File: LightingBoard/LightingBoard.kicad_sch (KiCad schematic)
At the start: 58 parts, among them J1 Barrel_Jack_Switch, J2 LED Out, J3 LED Out, J4 Programming, J5 UART, U1 AP7384-50SA, U2 NCV833, U3 INA180A2, U4 LMR33630ADDA, U5 MCP4725xxx-xCH, U6 INA180A2, U7 LMR33630ADDA, U8 MCP4725xxx-xCH, U9 ATtiny2313A-S

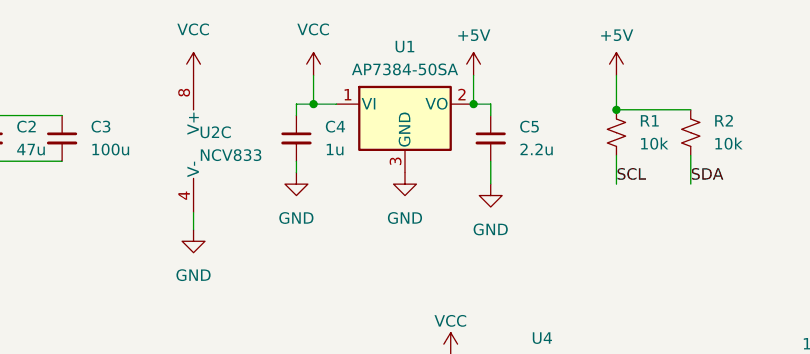
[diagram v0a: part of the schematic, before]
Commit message: add cost estimates
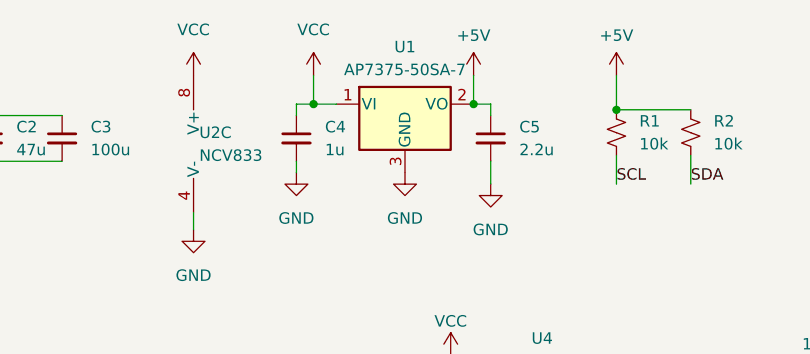
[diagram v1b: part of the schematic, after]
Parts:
- C1, C11, C12, C13, C14, C15, C17, C18, C4, C5, C6, C7, C8, C9, D1: Cost (none) -> .01
- C10, C16, C3: Cost (none) -> .183
- C2: Cost (none) -> 0
- L2, L4: Cost (none) -> .364
- R1, R10, R11, R13, R14, R15, R16, R17, R18, R19, R2, R20, R21, R4, R5, R6, R7, R8, R9: Cost (none) -> .005
- R12, R3: Cost (none) -> .052
- U1: value AP7384-50SA -> AP7375-50SA-7; Cost (none) -> .10
- U2: Cost (none) -> .225
- U3, U6: Cost (none) -> .131
- U4, U7: Cost (none) -> .927
- U5, U8: Cost (none) -> .949
- U9: Cost (none) -> 1.27

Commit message: NO MORR DINOSAURR
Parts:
- removed U1: AP7375-50SA-7, Package_TO_SOT_SMD:SOT-23, symbol Regulator_Linear:AP7384-50SA
- removed U9: ATtiny2313A-S, Package_SO:SOIC-20W_7.5x12.8mm_P1.27mm, symbol MCU_Microchip_ATtiny:ATtiny2313A-S
- added U10: AP2120N-5.0TRG1, Package_TO_SOT_SMD:SOT-23, symbol Regulator_Linear:MCP1700x-500xxTT
- added U9: ATtiny841-SS, Package_SO:SOIC-14_3.9x8.7mm_P1.27mm, symbol MCU_Microchip_ATtiny:ATtiny841-SS
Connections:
- net +5V: now also R11.2, U10.2 (VO), U9.1 (VCC); no longer R11.1
- net Enable1: now also U9.10 (PA3)
- net Enable2: now also U9.3 (XTAL2/PB1)
- net GND: now also C18.1, U10.1 (GND), U9.14 (GND); no longer C18.2
- net PG1: now also U9.13 (AREF/PA0)
- net PG2: now also U9.2 (XTAL1/PB0)
- net Reset: now also C18.2, R11.1, R20.2, U9.4 (~{RESET}/PB3); no longer C18.1, R11.2, R20.1
- net SCL: now also J4.2 (Pin_2), U9.9 (PA4); no longer J4.5 (Pin_5)
- net SDA: now also J4.4 (Pin_4), U9.7 (PA6); no longer J4.3 (Pin_3)
- net Status: now also U9.5 (PB2)
- net UART_RX: now also U9.11 (PA2)
- net UART_TX: now also U9.12 (PA1)
- net VCC: now also U10.3 (VI)
- new net CS(10): J4.5 (Pin_5), R20.1
- new net MISO(12): J4.3 (Pin_3), U9.8 (PA5)
- no-connect marks 6 -> 2
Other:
- moved on the sheet: C18, J4, J5, R11, R20

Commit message: fix some issues
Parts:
- C12, C6: value .1u -> 100nF
- R14, R5: value 4k -> 30k
- R18, R9: value 1k -> 10k
- U2: value NCV833 -> TL5580IDR
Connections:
- net +5V: now also C12.1, C6.1, U3.5 (V+), U6.5 (V+)
- net VCC: no longer C12.1, C6.1, U3.5 (V+), U6.5 (V+)
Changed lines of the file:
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@@
       (effects (font (size 1.27 1.27)) (justify left))
     )
-    (property "Value" ".1u" (at 205.74 113.6713 0)
+    (property "Value" "100nF" (at 205.74 113.6713 0)
       (effects (font (size 1.27 1.27)) (justify left))
     )
@@
       (effects (font (size 1.27 1.27)) (justify right))
     )
-    (property "Value" "4k" (at 276.225 133.985 0)
+    (property "Value" "30k" (at 276.225 133.985 0)
       (effects (font (size 1.27 1.27)) (justify right))
     )
@@
       (effects (font (size 1.27 1.27)) hide)
     )
-    (property "Datasheet" "~" (at 274.32 132.715 0)
+    (property "Datasheet" "RT0603FRE0730KL " (at 274.32 132.715 0)
       (effects (font (size 1.27 1.27)) hide)
     )
@@
         (path "/3512c088-bc62-4a72-803d-5db96724f2eb"
           (reference "#PWR025") (unit 1)
-        )
-      )
-    )
-  )
-  (symbol (lib_id "power:VCC") (at 195.58 49.53 0) (unit 1)
-    (in_bom yes) (on_board yes) (dnp no)
-    (property "Reference" "#PWR014" (at 195.58 53.34 0)
-      (effects (font (size 1.27 1.27)) hide)
-    )
-    (property "Value" "VCC" (at 195.58 45.72 0)
-      (effects (font (size 1.27 1.27)))
-    )
-    (property "Footprint" "" (at 195.58 49.53 0)
-      (effects (font (size 1.27 1.27)) hide)
-    )
-    (property "Datasheet" "" (at 195.58 49.53 0)
-      (effects (font (size 1.27 1.27)) hide)
-    )
-    (pin "1")
-    (instances
-      (project "LightingBoard"
-        (path "/3512c088-bc62-4a72-803d-5db96724f2eb"
-          (reference "#PWR014") (unit 1)
         )
       )
@@
       (effects (font (size 1.27 1.27)) (justify right))
     )
-    (property "Value" "1k" (at 274.955 74.295 0)
+    (property "Value" "10k" (at 274.955 74.295 0)
       (effects (font (size 1.27 1.27)) (justify right))
     )
@@
     )
   )
-  (symbol (lib_id "power:VCC") (at 201.295 41.275 0) (unit 1)
-    (in_bom yes) (on_board yes) (dnp no)
-    (property "Reference" "#PWR011" (at 201.295 45.085 0)
-      (effects (font (size 1.27 1.27)) hide)
-    )
-    (property "Value" "VCC" (at 201.295 37.465 0)
-      (effects (font (size 1.27 1.27)))
-    )
-    (property "Footprint" "" (at 201.295 41.275 0)
-      (effects (font (size 1.27 1.27)) hide)
-    )
-    (property "Datasheet" "" (at 201.295 41.275 0)
-      (effects (font (size 1.27 1.27)) hide)
-    )
-    (pin "1")
-    (instances
-      (project "LightingBoard"
-        (path "/3512c088-bc62-4a72-803d-5db96724f2eb"
-          (reference "#PWR011") (unit 1)
-        )
-      )
-    )
-  )
   (symbol (lib_id "Device:C_Small") (at 162.56 130.81 0) (unit 1)
     (in_bom yes) (on_board yes) (dnp no) (fields_autoplaced)
@@
     )
   )
+  (symbol (lib_id "power:+5V") (at 196.85 118.11 0) (unit 1)
+    (in_bom yes) (on_board yes) (dnp no) (fields_autoplaced)
+    (property "Reference" "#PWR011" (at 196.85 121.92 0)
+      (effects (font (size 1.27 1.27)) hide)
+    )
+    (property "Value" "+5V" (at 196.85 113.665 0)
+      (effects (font (size 1.27 1.27)))
+    )
+    (property "Footprint" "" (at 196.85 118.11 0)
+      (effects (font (size 1.27 1.27)) hide)
+    )
+    (property "Datasheet" "" (at 196.85 118.11 0)
+      (effects (font (size 1.27 1.27)) hide)
+    )
+    (pin "1")
+    (instances
+      (project "LightingBoard"
+        (path "/3512c088-bc62-4a72-803d-5db96724f2eb"
+          (reference "#PWR011") (unit 1)
+        )
+      )
+    )
+  )
   (symbol (lib_id "power:GND") (at 172.085 62.23 0) (unit 1)
     (in_bom yes) (on_board yes) (dnp no) (fields_autoplaced)
@@
       (effects (font (size 1.27 1.27)) (justify left))
     )
-    (property "Value" "NCV833" (at 70.485 27.305 0)
+    (property "Value" "TL5580IDR" (at 70.485 27.305 0)
       (effects (font (size 1.27 1.27)) (justify left))
     )
@@
     )
   )
-  (symbol (lib_id "power:VCC") (at 196.85 118.11 0) (unit 1)
-    (in_bom yes) (on_board yes) (dnp no)
-    (property "Reference" "#PWR030" (at 196.85 121.92 0)
-      (effects (font (size 1.27 1.27)) hide)
-    )
-    (property "Value" "VCC" (at 196.85 114.3 0)
-      (effects (font (size 1.27 1.27)))
-    )
-    (property "Footprint" "" (at 196.85 118.11 0)
-      (effects (font (size 1.27 1.27)) hide)
-    )
-    (property "Datasheet" "" (at 196.85 118.11 0)
-      (effects (font (size 1.27 1.27)) hide)
-    )
-    (pin "1")
-    (instances
-      (project "LightingBoard"
-        (path "/3512c088-bc62-4a72-803d-5db96724f2eb"
-          (reference "#PWR030") (unit 1)
-        )
-      )
-    )
-  )
   (symbol (lib_id "Device:R_Small_US") (at 241.935 125.73 270) (unit 1)
     (in_bom yes) (on_board yes) (dnp no) (fields_autoplaced)
@@
     )
   )
+  (symbol (lib_id "power:+5V") (at 202.565 109.855 0) (unit 1)
+    (in_bom yes) (on_board yes) (dnp no) (fields_autoplaced)
+    (property "Reference" "#PWR014" (at 202.565 113.665 0)
+      (effects (font (size 1.27 1.27)) hide)
+    )
+    (property "Value" "+5V" (at 202.565 105.41 0)
+      (effects (font (size 1.27 1.27)))
+    )
+    (property "Footprint" "" (at 202.565 109.855 0)
+      (effects (font (size 1.27 1.27)) hide)
+    )
+    (property "Datasheet" "" (at 202.565 109.855 0)
+      (effects (font (size 1.27 1.27)) hide)
+    )
+    (pin "1")
+    (instances
+      (project "LightingBoard"
+        (path "/3512c088-bc62-4a72-803d-5db96724f2eb"
+          (reference "#PWR014") (unit 1)
+        )
+      )
+    )
+  )
   (symbol (lib_id "power:GND") (at 196.85 134.62 0) (unit 1)
     (in_bom yes) (on_board yes) (dnp no)
@@
     )
   )
-  (symbol (lib_id "power:VCC") (at 202.565 109.855 0) (unit 1)
-    (in_bom yes) (on_board yes) (dnp no)
-    (property "Reference" "#PWR026" (at 202.565 113.665 0)
-      (effects (font (size 1.27 1.27)) hide)
-    )
-    (property "Value" "VCC" (at 202.565 106.045 0)
-      (effects (font (size 1.27 1.27)))
-    )
-    (property "Footprint" "" (at 202.565 109.855 0)
-      (effects (font (size 1.27 1.27)) hide)
-    )
-    (property "Datasheet" "" (at 202.565 109.855 0)
-      (effects (font (size 1.27 1.27)) hide)
-    )
-    (pin "1")
-    (instances
-      (project "LightingBoard"
-        (path "/3512c088-bc62-4a72-803d-5db96724f2eb"
-          (reference "#PWR026") (unit 1)
-        )
-      )
-    )
-  )
   (symbol (lib_id "Device:R_Small_US") (at 130.175 137.16 90) (unit 1)
     (in_bom yes) (on_board yes) (dnp no) (fields_autoplaced)
@@
     )
   )
+  (symbol (lib_id "power:+5V") (at 195.58 49.53 0) (unit 1)
+    (in_bom yes) (on_board yes) (dnp no) (fields_autoplaced)
+    (property "Reference" "#PWR026" (at 195.58 53.34 0)
+      (effects (font (size 1.27 1.27)) hide)
+    )
+    (property "Value" "+5V" (at 195.58 45.085 0)
+      (effects (font (size 1.27 1.27)))
+    )
+    (property "Footprint" "" (at 195.58 49.53 0)
+      (effects (font (size 1.27 1.27)) hide)
+    )
+    (property "Datasheet" "" (at 195.58 49.53 0)
+      (effects (font (size 1.27 1.27)) hide)
+    )
+    (pin "1")
+    (instances
+      (project "LightingBoard"
+        (path "/3512c088-bc62-4a72-803d-5db96724f2eb"
+          (reference "#PWR026") (unit 1)
+        )
+      )
+    )
+  )
   (symbol (lib_id "Device:R_Small_US") (at 240.665 57.15 270) (unit 1)
     (in_bom yes) (on_board yes) (dnp no) (fields_autoplaced)
@@
       (effects (font (size 1.27 1.27)))
     )
-    (property "Value" "NCV833" (at 259.715 120.65 0)
+    (property "Value" "TL5580IDR" (at 259.715 120.65 0)
       (effects (font (size 1.27 1.27)))
     )
@@
       (effects (font (size 1.27 1.27)) (justify right))
     )
-    (property "Value" "4k" (at 274.955 65.405 0)
+    (property "Value" "30k" (at 274.955 65.405 0)
       (effects (font (size 1.27 1.27)) (justify right))
     )
@@
       (effects (font (size 1.27 1.27)) hide)
     )
-    (property "Datasheet" "~" (at 273.05 64.135 0)
+    (property "Datasheet" "RT0603FRE0730KL " (at 273.05 64.135 0)
       (effects (font (size 1.27 1.27)) hide)
     )
@@
       (effects (font (size 1.27 1.27)))
     )
-    (property "Value" "NCV833" (at 258.445 52.705 0)
+    (property "Value" "TL5580IDR" (at 258.445 52.705 0)
       (effects (font (size 1.27 1.27)))
     )
@@
     )
   )
+  (symbol (lib_id "power:+5V") (at 201.295 41.275 0) (unit 1)
+    (in_bom yes) (on_board yes) (dnp no) (fields_autoplaced)
+    (property "Reference" "#PWR030" (at 201.295 45.085 0)
+      (effects (font (size 1.27 1.27)) hide)
+    )
+    (property "Value" "+5V" (at 201.295 36.83 0)
+      (effects (font (size 1.27 1.27)))
+    )
+    (property "Footprint" "" (at 201.295 41.275 0)
+      (effects (font (size 1.27 1.27)) hide)
+    )
+    (property "Datasheet" "" (at 201.295 41.275 0)
+      (effects (font (size 1.27 1.27)) hide)
+    )
+    (pin "1")
+    (instances
+      (project "LightingBoard"
+        (path "/3512c088-bc62-4a72-803d-5db96724f2eb"
+          (reference "#PWR030") (unit 1)
+        )
+      )
+    )
+  )
   (symbol (lib_id "Device:C_Small") (at 146.685 130.81 0) (unit 1)
     (in_bom yes) (on_board yes) (dnp no) (fields_autoplaced)
@@
       (effects (font (size 1.27 1.27)) (justify right))
     )
-    (property "Value" "1k" (at 276.225 142.875 0)
+    (property "Value" "10k" (at 276.225 142.875 0)
       (effects (font (size 1.27 1.27)) (justify right))
     )
@@
       (effects (font (size 1.27 1.27)) (justify left))
     )
-    (property "Value" ".1u" (at 204.47 45.0913 0)
-      (effects (font (size 1.27 1.27)) (justify left))
-    )
+    (property "Value" "100nF" (at 204.47 45.0913 0)
+      (effects (font (size 1.27 1.27)) (justify left))
+    )

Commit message: HEHEHE
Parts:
- added C19, C21, C24: 100nF, Capacitor_SMD:C_0603_1608Metric, symbol Device:C_Small
- added C20, C22: 10uF, Capacitor_SMD:C_0603_1608Metric, symbol Device:C_Small
- added C23: 1u, Capacitor_SMD:C_0603_1608Metric, symbol Device:C_Small
- C2: value 47u -> 10u
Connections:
- net +5V: now also C19.1, C20.1, C21.1, C22.1
- net GND: now also C19.2, C20.2, C21.2, C22.2, C23.2, C24.2
- net VCC: now also C23.1, C24.1
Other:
- moved on the sheet: C12, C4, C5, R1, R2, U10, U2C

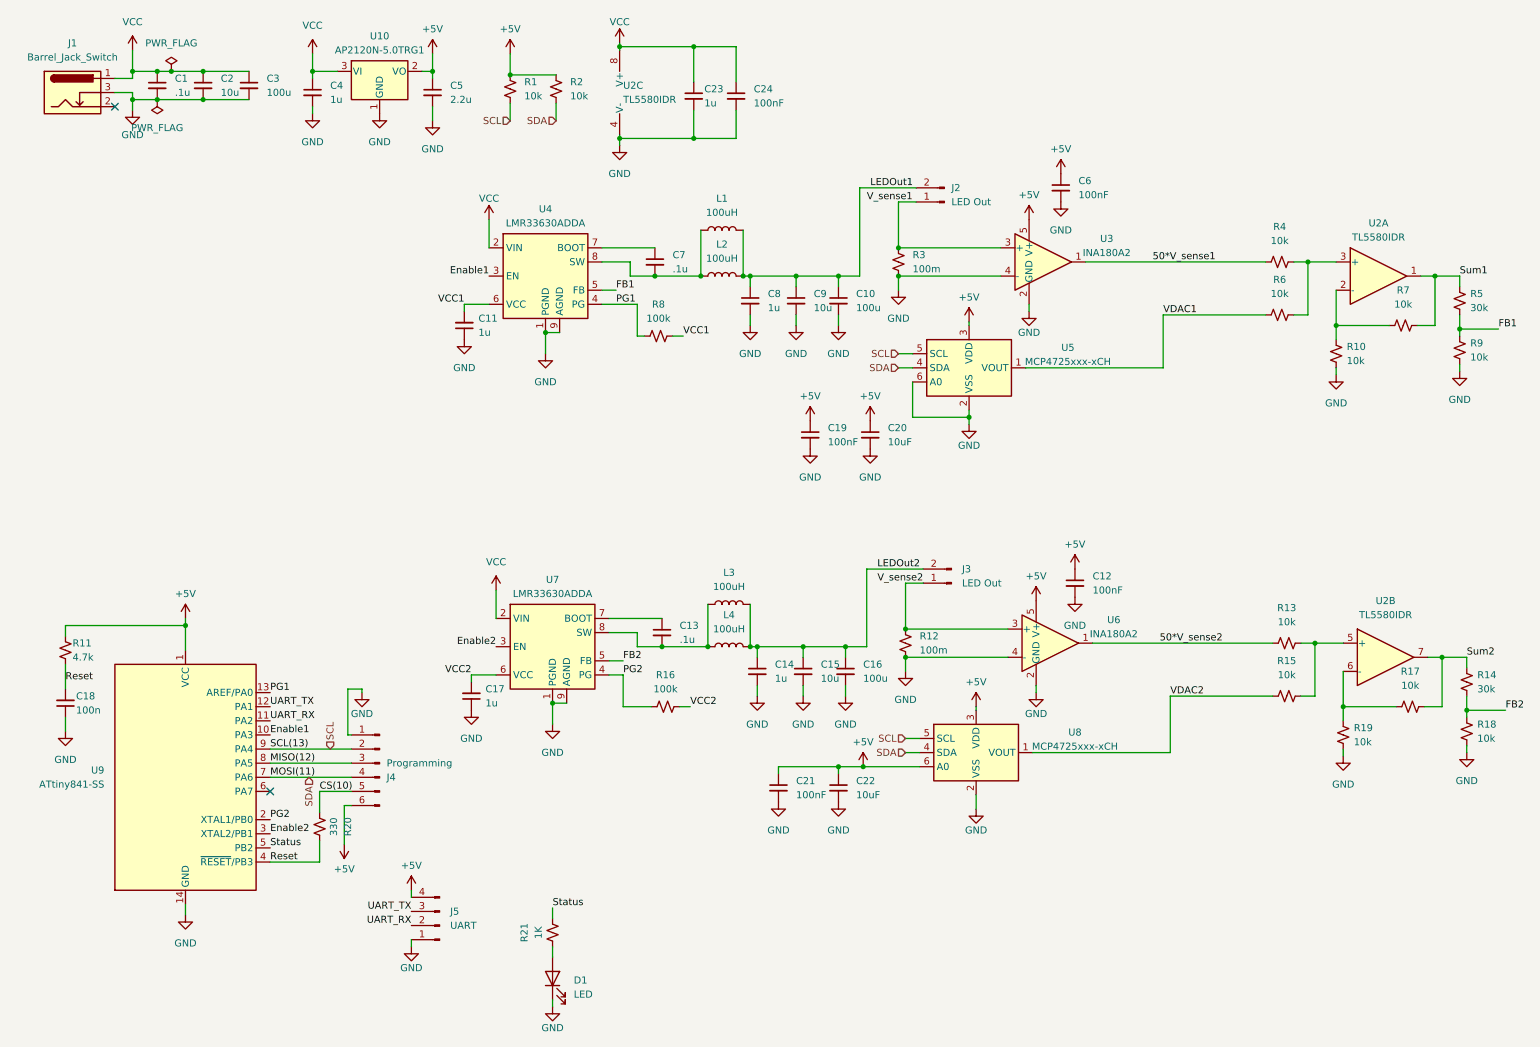
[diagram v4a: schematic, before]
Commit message: new design based on AVR32DD20
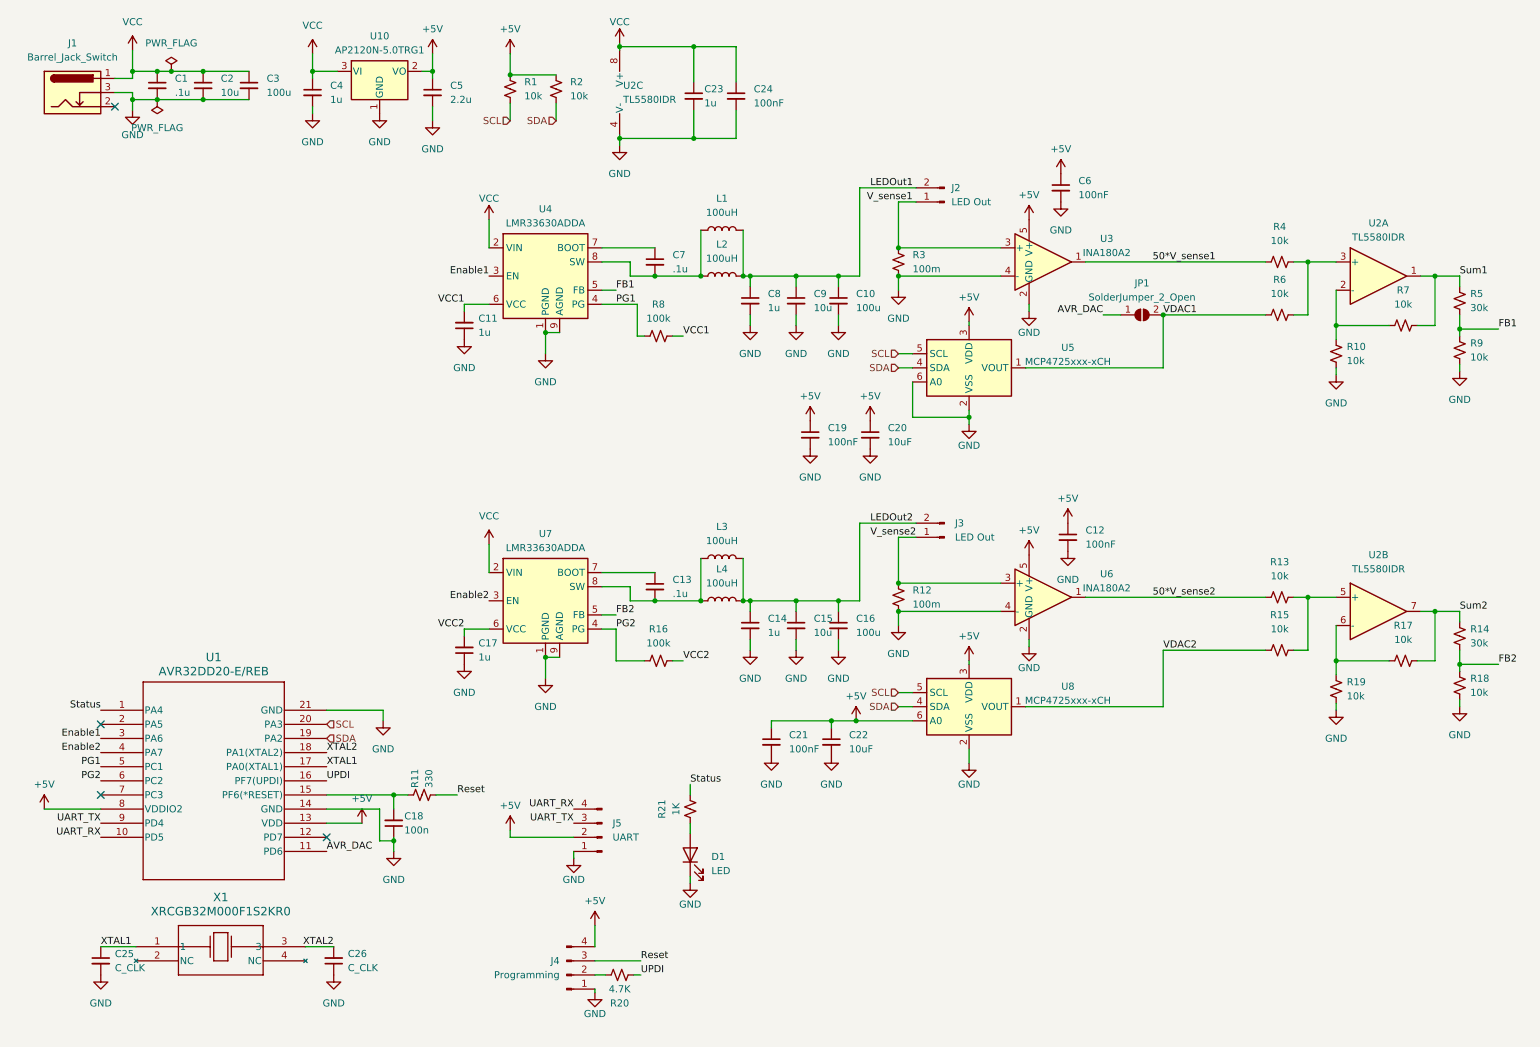
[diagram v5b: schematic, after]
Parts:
- removed U9: ATtiny841-SS, Package_SO:SOIC-14_3.9x8.7mm_P1.27mm, symbol MCU_Microchip_ATtiny:ATtiny841-SS
- added C25, C26: C_CLK, Capacitor_SMD:C_0603_1608Metric, symbol Device:C_Small
- added JP1: SolderJumper_2_Open, Jumper:SolderJumper-2_P1.3mm_Open_RoundedPad1.0x1.5mm, symbol Jumper:SolderJumper_2_Open
- added U1: AVR32DD20-E/REB, Package_DFN_QFN:VQFN-20-1EP_3x3mm_P0.4mm_EP1.7x1.7mm, symbol CustomSymbols:AVR32DD20-E_REB
- added X1: XRCGB32M000F1S2KR0, Crystal:Crystal_SMD_2016-4Pin_2.0x1.6mm, symbol CustomSymbols:XRCGB32M000F1S2KR0
- J4: footprint Connector_PinSocket_2.54mm:PinSocket_1x06_P2.54mm_Vertical -> Connector_PinSocket_2.54mm:PinSocket_1x04_P2.54mm_Vertical; symbol Connector:Conn_01x06_Pin -> Connector:Conn_01x04_Pin
- J5: footprint Connector_PinSocket_2.54mm:PinSocket_1x04_P2.54mm_Vertical -> Connector_JST:JST_SH_BM04B-SRSS-TB_1x04-1MP_P1.00mm_Vertical
- L1, L3: footprint BuckParts:7447231101 -> CustomFootprints:7447231101
- L2, L4: footprint BuckParts:IND_BOURNS_SDR1307 -> CustomFootprints:IND_BOURNS_SDR1307
- R11: value 4.7k -> 330
- R20: value 330 -> 4.7K
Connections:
- net MISO(12) is gone; now on net Reset: J4.3 (Pin_3)
- net +5V: now also J4.4 (Pin_4), J5.2 (Pin_2), U1.13 (VDD), U1.8 (VDDIO2); no longer J4.6 (Pin_6), J5.4 (Pin_4), R11.2
- net Enable1: now also U1.3 (PA6)
- net Enable2: now also U1.4 (PA7)
- net GND: now also C25.2, C26.1, U1.14 (GND), U1.21 (GND)
- net PG1: now also U1.5 (PC1)
- net PG2: now also U1.6 (PC2)
- net Reset: no longer C18.2, R20.2
- net SCL: now also U1.20 (PA3); no longer J4.2 (Pin_2)
- net SDA: now also U1.19 (PA2); no longer J4.4 (Pin_4)
- net Status: now also U1.1 (PA4)
- net UART_RX: now also J5.4 (Pin_4), U1.10 (PD5); no longer J5.2 (Pin_2)
- net UART_TX: now also U1.9 (PD4)
- net VDAC1: now also JP1.2 (B)
- net CS(10) renamed UPDI
- net UPDI: now also U1.16 (PF7(UPDI)); no longer J4.5 (Pin_5)
- new net: J4.2 (Pin_2), R20.2
- new net: C18.2, R11.2, U1.15 (PF6(*RESET))
- new net AVR_DAC: JP1.1 (A), U1.11 (PD6)
- new net XTAL1: C25.1, U1.17 (PA0(XTAL1)), X1.1
- new net XTAL2: C26.2, U1.18 (PA1(XTAL2)), X1.3
- no-connect marks 2 -> 4
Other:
- moved on the sheet: C12, C13, C14, C15, C16, C17, C18, C21, C22, D1, J3, J5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
